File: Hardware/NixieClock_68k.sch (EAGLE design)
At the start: 71 parts, among them IC1 68008, IC11 NE555, IC12 74HC08N, IC13 74HC05, IC2 AS6C1008, IC3 39SF020, IC4 DS1244Y, IC5 68681, IC6 74HC30N, IC7 74HC04N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

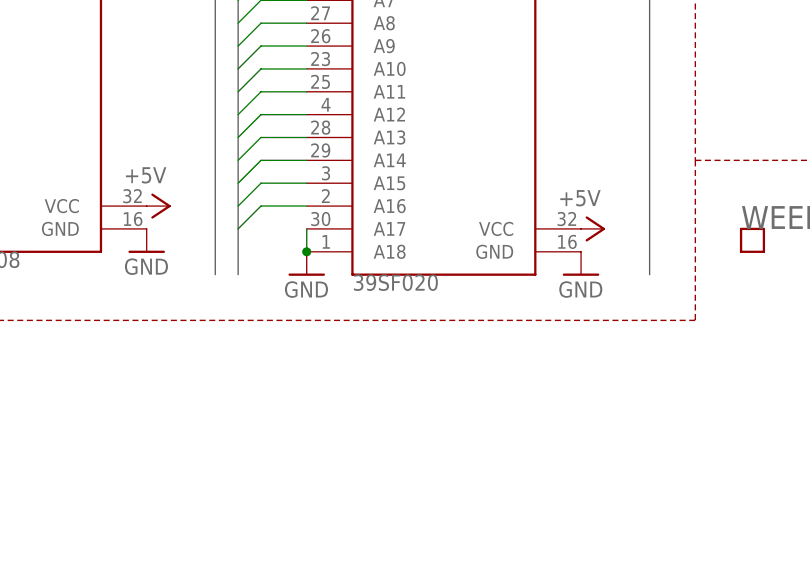
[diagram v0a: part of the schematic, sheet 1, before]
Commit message: more uart stuff in loader
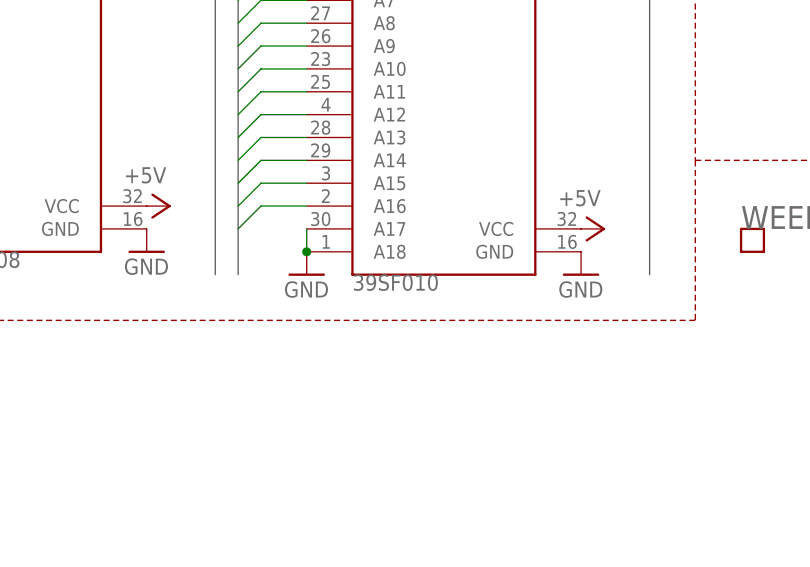
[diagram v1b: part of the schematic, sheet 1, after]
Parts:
- IC3: value 39SF020 -> 39SF010; MOUSER (none) -> 804-39SF010A7CPHE
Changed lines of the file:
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@@
 <?xml version="1.0" encoding="utf-8"?>
 <!DOCTYPE eagle SYSTEM "eagle.dtd">
-<eagle version="9.3.0">
+<eagle version="9.3.2">
 <drawing>
 <settings>
@@
 <part name="GND2" library="supply1" library_urn="urn:adsk.eagle:library:371" deviceset="GND" device=""/>
 <part name="IC2" library="Parts" deviceset="AS6C1008" device="" package3d_urn="urn:adsk.eagle:package:18076/2" value="AS6C1008"/>
-<part name="IC3" library="Parts" deviceset="SST39SF0X0" device="PDIP32" package3d_urn="urn:adsk.eagle:package:18076/2" value="39SF020"/>
+<part name="IC3" library="Parts" deviceset="SST39SF0X0" device="PDIP32" package3d_urn="urn:adsk.eagle:package:18076/2" value="39SF010">
+<attribute name="MOUSER" value="804-39SF010A7CPHE"/>
+</part>
 <part name="P+3" library="supply1" library_urn="urn:adsk.eagle:library:371" deviceset="+5V" device=""/>
 <part name="P+4" library="supply1" library_urn="urn:adsk.eagle:library:371" deviceset="+5V" device=""/>
